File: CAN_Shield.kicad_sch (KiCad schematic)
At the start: 24 parts, among them J1 GPIO, J2 Screw_Terminal_01x02, J3 Screw_Terminal_01x02, U1 CAT24C256, U2 MCP2515-xSO, U3 SN65HVD231, U4 SN65HVD230DR, X1 X322516MLB4SI, Y1 Crystal

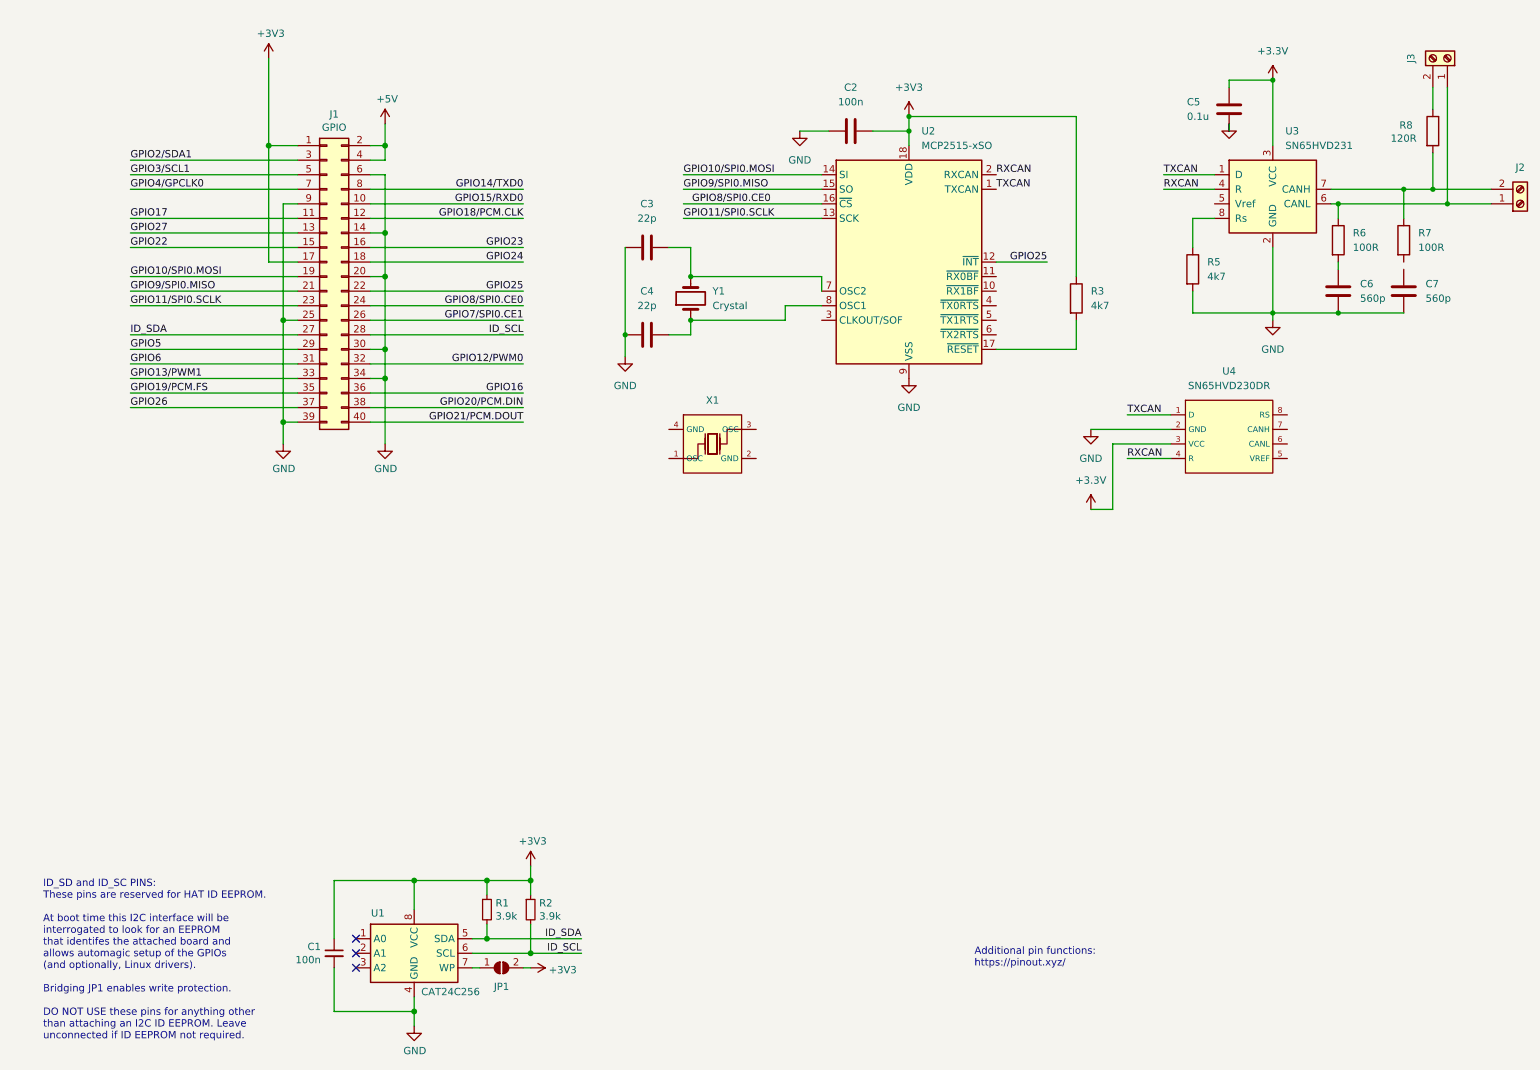
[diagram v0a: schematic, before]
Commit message: finished layout with 9 pin screw terminal, Unfinished edge extend and diff pair CAN
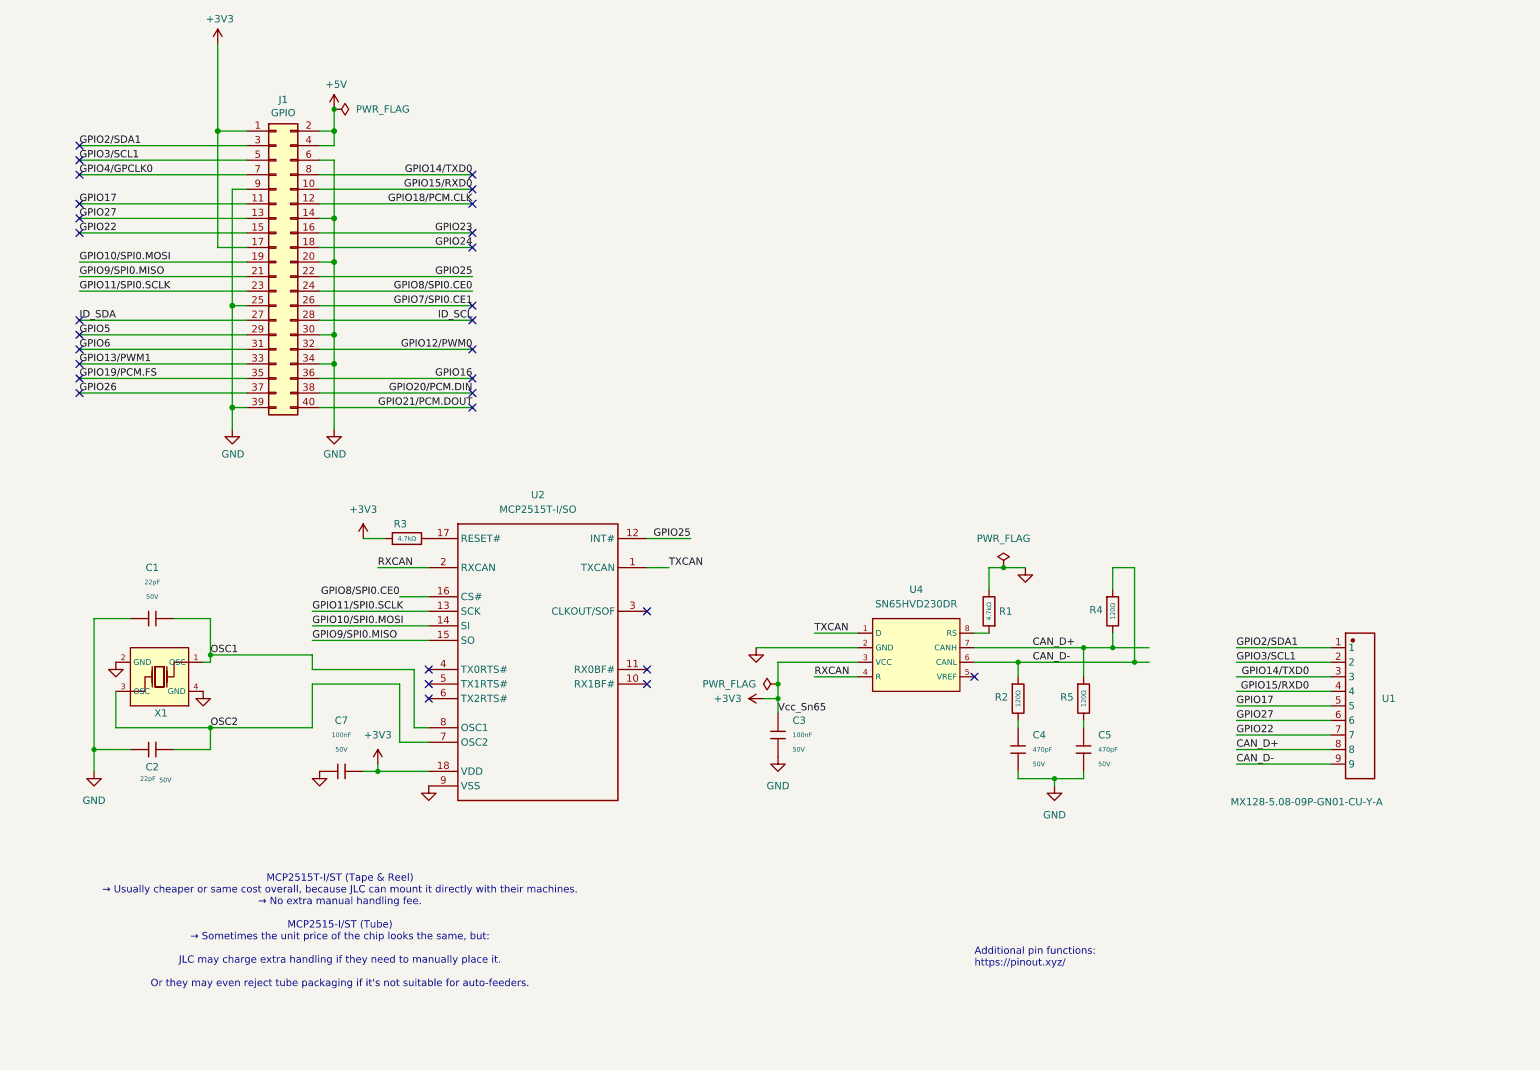
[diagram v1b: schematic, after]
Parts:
- removed C1: 100n, Capacitor_SMD:C_0402_1005Metric, symbol Device:C_Small
- removed C2: 100n, Capacitor_SMD:C_0402_1005Metric, symbol Device:C
- removed C3, C4: 22p, Capacitor_SMD:C_0402_1005Metric, symbol Device:C
- removed C5: 0.1u, Capacitor_SMD:C_0402_1005Metric, symbol Device:C
- removed C6, C7: 560p, Capacitor_SMD:C_0402_1005Metric, symbol Device:C
- removed J2: Screw_Terminal_01x02, TerminalBlock_Wuerth:Wuerth_REDCUBE-THR_WP-THRBU_74655095_THR, symbol Connector:Screw_Terminal_01x02
- removed J3: Screw_Terminal_01x02, TerminalBlock_Wuerth:Wuerth_REDCUBE-THR_WP-THRBU_74650173_THR, symbol Connector:Screw_Terminal_01x02
- removed JP1: ID_WP, symbol Jumper:SolderJumper_2_Open
- removed R1, R2: 3.9k, Resistor_SMD:R_0402_1005Metric, symbol Device:R_Small
- removed R3, R5: 4k7, Resistor_SMD:R_0402_1005Metric, symbol Device:R
- removed R6, R7: 100R, Resistor_SMD:R_0402_1005Metric, symbol Device:R
- removed R8: 120R, Resistor_SMD:R_0402_1005Metric, symbol Device:R
- removed U1: CAT24C256, symbol Memory_EEPROM:CAT24C256
- removed U2: MCP2515-xSO, Package_SO:SOIC-18W_7.5x11.6mm_P1.27mm, symbol Interface_CAN_LIN:MCP2515-xSO
- removed U3: SN65HVD231, Package_SO:SOIC-8_3.9x4.9mm_P1.27mm, symbol Interface_CAN_LIN:SN65HVD231
- removed Y1: Crystal, Crystal:Crystal_SMD_3225-4Pin_3.2x2.5mm, symbol Device:Crystal
- added C1, C2: 22pF, PCM_JLCPCB:C_0402, symbol PCM_JLCPCB-Capacitors:0402,22pF
- added C3, C7: 100nF, PCM_JLCPCB:C_0603, symbol PCM_JLCPCB-Capacitors:0603,100nF
- added C4, C5: 470pF, PCM_JLCPCB:C_0402, symbol PCM_JLCPCB-Capacitors:0402,470pF
- added R1, R3: 4.7kΩ, PCM_JLCPCB:R_0402, symbol PCM_JLCPCB-Resistors:0402,4.7kΩ
- added R2, R4, R5: 120Ω, PCM_JLCPCB:R_0603, symbol PCM_JLCPCB-Resistors:0603,120Ω
- added U1: MX128-5.08-09P-GN01-CU-Y-A, ImportFP:CONN-TH_9P-P5.08_MX128-5.08-09P-GN01-CU-Y-A, symbol ImportSymbol:MX128-5.08-09P-GN01-CU-Y-A
- added U2: MCP2515T-I/SO, ImportFP:MCP2515T-IST_SOIC-18_L11.6-W7.5-P1.27-LS10.3-BL, symbol ImportSymbol:MCP2515T-I/SO
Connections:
- net +3.3V is gone; now on net +3V3: U4.3 (VCC)
- net +3V3: now also C3.1, C7.2, R3.1, U2.18 (VDD)
- net GND: now also X1.2 (GND), X1.4 (GND), C1.1, C2.1, C3.2, C4.2, C5.2, C7.1, R1.2, U2.9 (VSS)
- net GPIO10/SPI0.MOSI: now also U2.14 (SI)
- net GPIO11/SPI0.SCLK: now also U2.13 (SCK)
- net GPIO14/TXD0: now also U1.3
- net GPIO15/RXD0: now also U1.4
- net GPIO17: now also U1.5
- net GPIO22: now also U1.7
- net GPIO25: now also U2.12 (INT#)
- net GPIO27: now also U1.6
- net GPIO2/SDA1: now also U1.1
- net GPIO3/SCL1: now also U1.2
- net GPIO8/SPI0.CE0: now also U2.16 (CS#)
- net GPIO9/SPI0.MISO: now also U2.15 (SO)
- net RXCAN: now also U2.2 (RXCAN)
- net TXCAN: now also U2.1 (TXCAN)
- net OSC1: now reaches X1.1 (OSC)
- net OSC1: now also C1.2, U2.8 (OSC1)
- net OSC2: now reaches X1.3 (OSC)
- net OSC2: now also C2.2, U2.7 (OSC2)
- net CAN_D-: now reaches U4.6 (CANL)
- net CAN_D-: now also R2.1, R4.1, U1.9
- net CAN_D+: now reaches U4.7 (CANH)
- net CAN_D+: now also R4.2, R5.1, U1.8
- net at U4.8 (RS): now also R1.1
- new net: C5.1, R5.2
- new net: C4.1, R2.2
- new net: R3.2, U2.17 (RESET#)
- no-connect marks 3 -> 30
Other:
- note added: "MCP2515T-I/ST (Tape & Reel) → Usually cheaper or same cost overall, because JLC can mount it directly with their machines. → No extra manual handling fee. MCP2515-I/ST (Tube) → Sometimes the unit price of the chip looks the same, but: JLC may charge extra handling if they need to manually place it. Or they may even reject tube packaging if it's not suitable for auto-feeders."
- note removed: "ID_SD and ID_SC PINS: These pins are reserved for HAT ID EEPROM. At boot time this I2C interface will be interrogated to look for an EEPROM that identifes the attached board and allows automagic setup of the GPIOs (and optionally, Linux drivers). Bridging JP1 enables write protection. DO NOT USE these pins for anything other than attaching an I2C ID EEPROM. Leave unconnected if ID EEPROM not requ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"
- moved on the sheet: J1, U4
